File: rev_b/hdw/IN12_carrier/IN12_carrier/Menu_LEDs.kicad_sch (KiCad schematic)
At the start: 28 parts, among them U1002 24AA02-OT, U501 TCA9555RGER

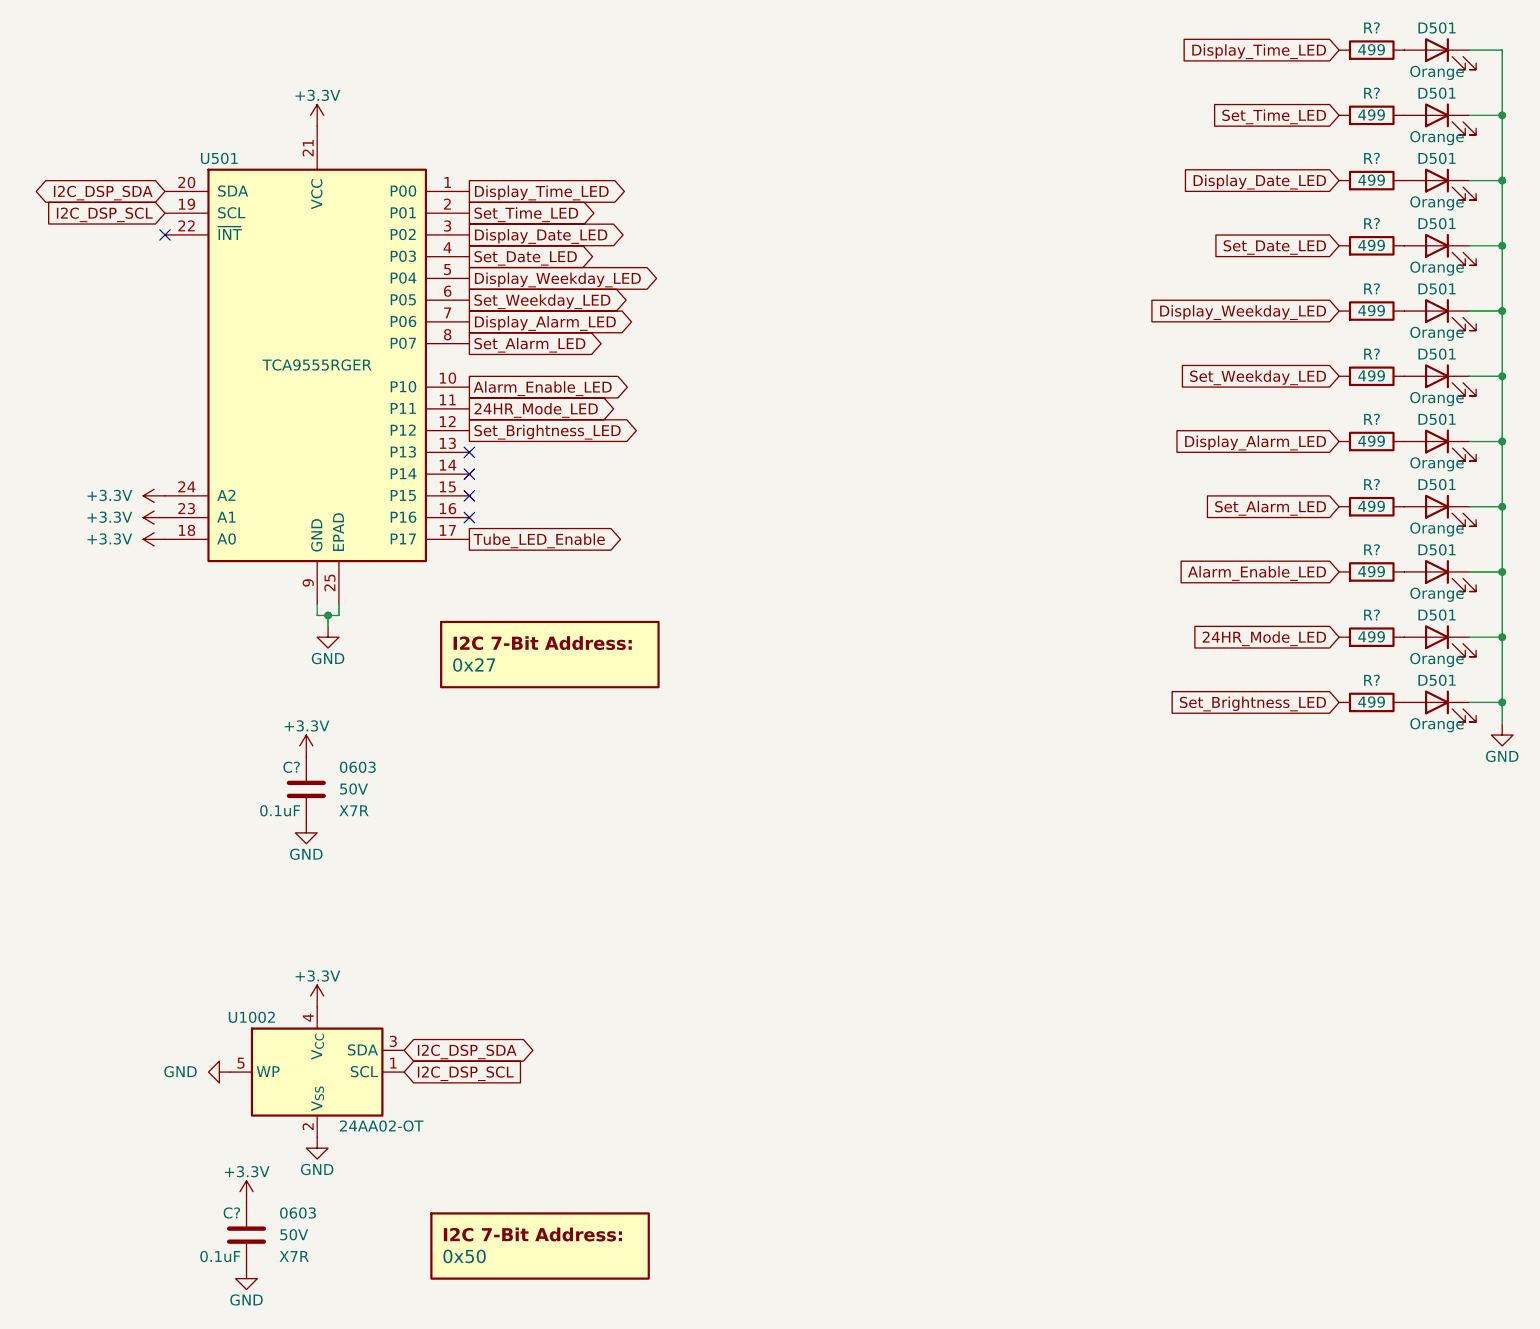
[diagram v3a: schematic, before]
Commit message: added BOM for IN12 carrier, finished routing, some schematic tweaks, adjusted design rules for ERC
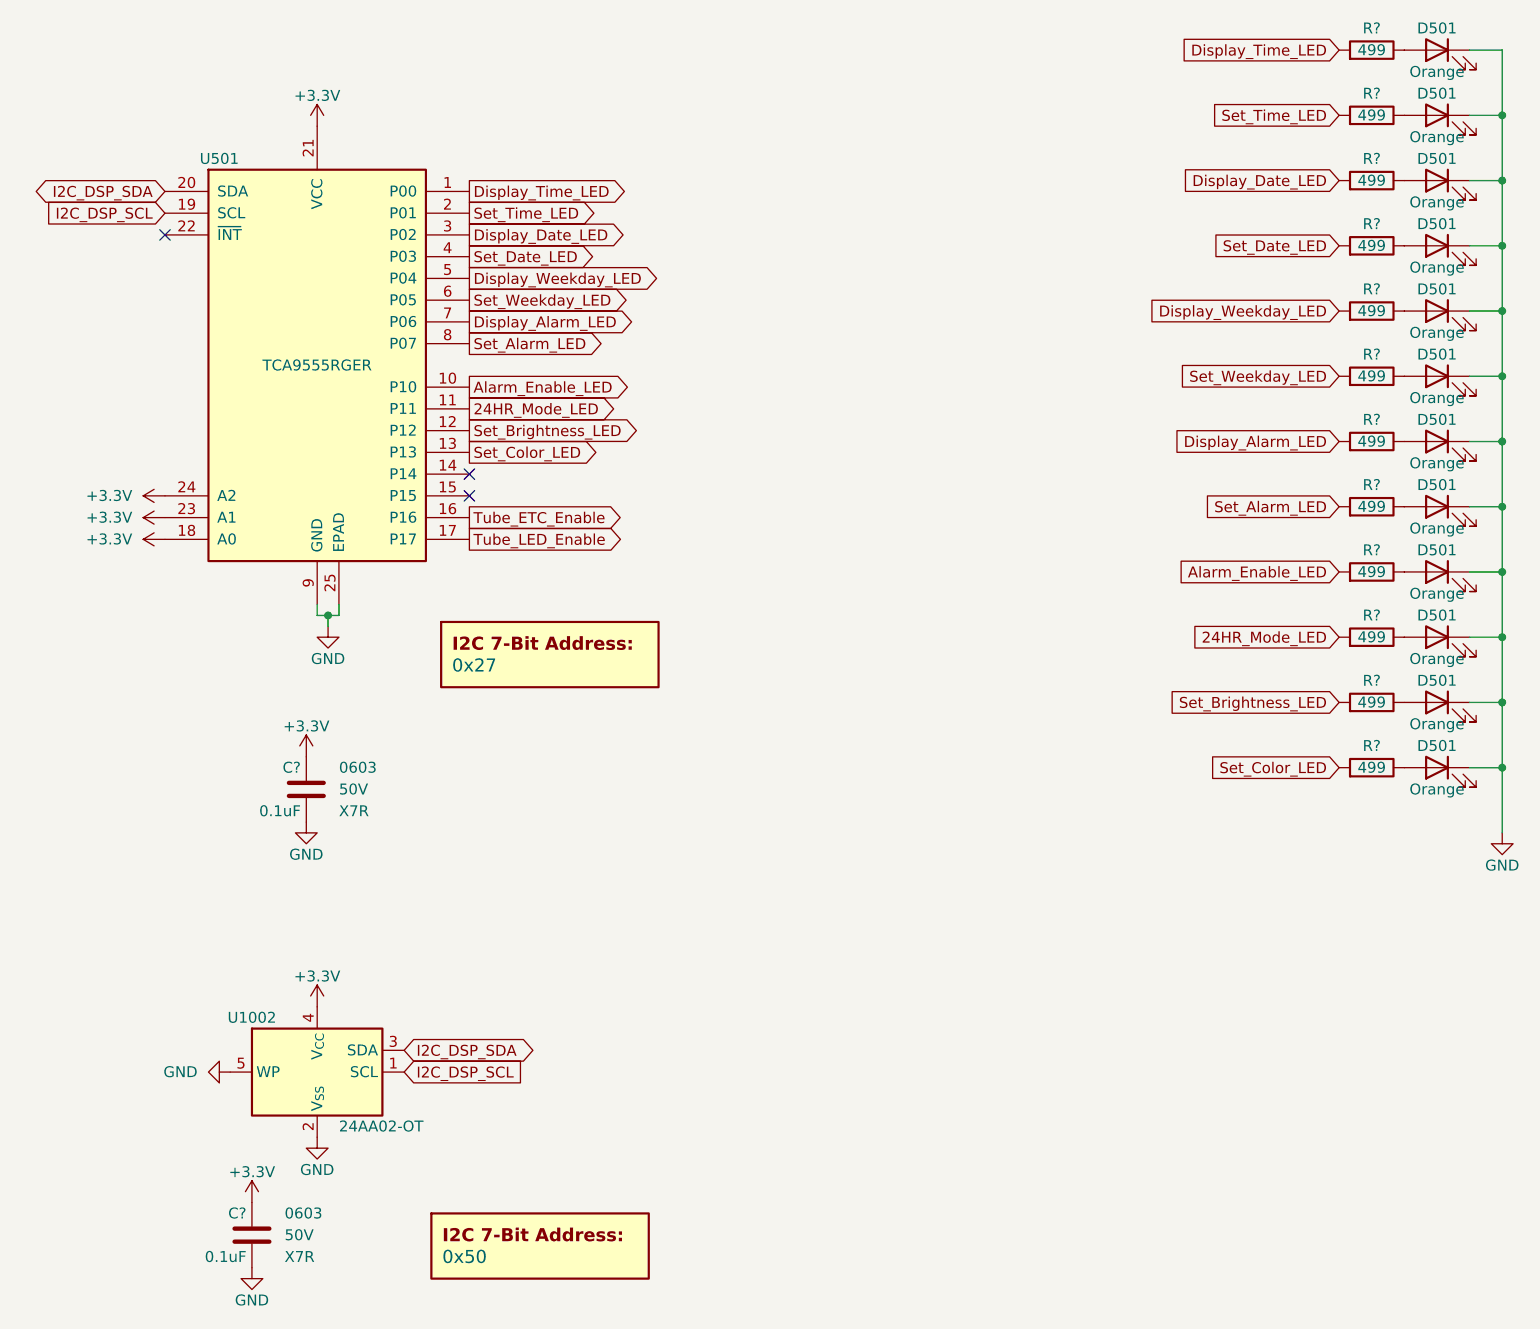
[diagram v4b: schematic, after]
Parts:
- added D501: Orange, LEDs:LED_0603, symbol Device:LED
- added R?: 499, Resistors_SMD:R_0603, symbol Custom_Library:R_Custom
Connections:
- net GND: now also D501.1 (K)
- net Set_Color_LED: now reaches U501.13 (P13)
- net Set_Color_LED: now also R?.1
- net Tube_ETC_Enable: now reaches U501.16 (P16)
- new net: D501.2 (A), R?.2
- no-connect marks 5 -> 3
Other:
- moved on the sheet: C?

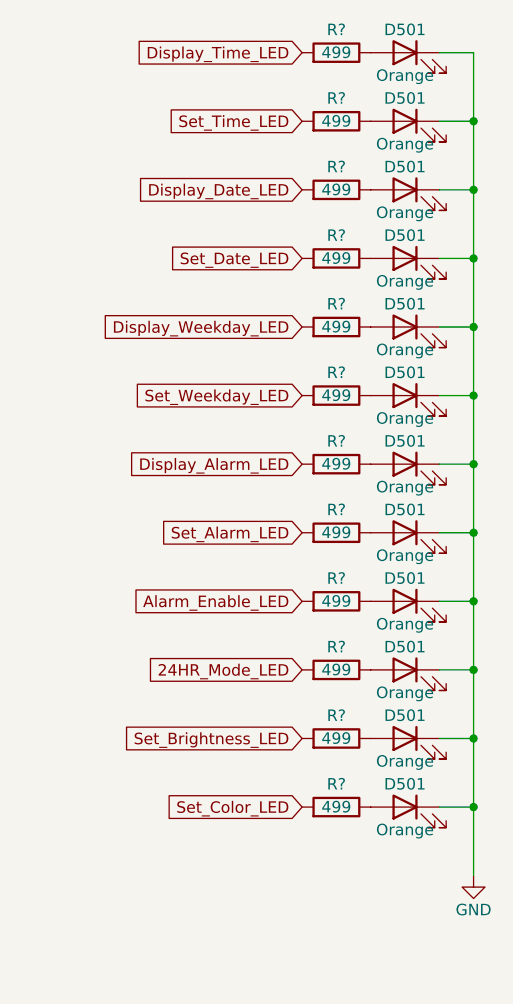
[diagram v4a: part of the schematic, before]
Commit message: assigned digikey pns to IN12 carrier board parts
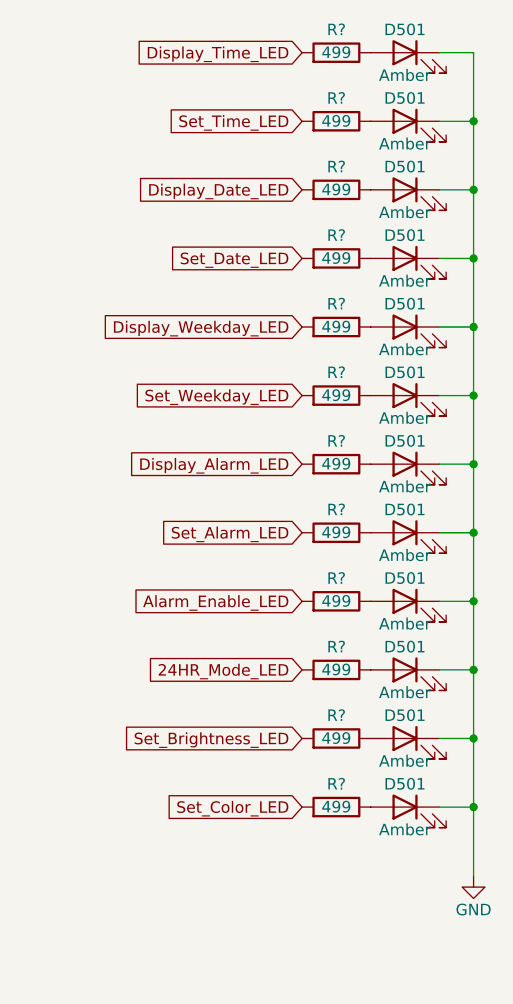
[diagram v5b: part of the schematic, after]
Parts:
- C? (x2): Digi-Key PN (none) -> 1276-CL10B104KB8NNNLCT-ND
- D501: value Orange -> Amber; Digi-Key PN (none) -> 732-150060AS75000CT-ND
- R? (x12): Digi-Key PN (none) -> 541-CRCW0603499RFKEBCT-ND
- U1002: Digi-Key PN (none) -> 24AA02E64T-I/OT
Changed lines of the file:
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@@
       (effects (font (size 1.27 1.27)))
     )
-    (property "Value" "Orange" (at 210.82 82.55 0)
+    (property "Value" "Amber" (at 210.82 82.55 0)
       (effects (font (size 1.27 1.27)))
     )
@@
       (effects (font (size 1.27 1.27)) hide)
     )
-    (property "Digi-Key PN" "" (at 210.82 80.01 0)
+    (property "Digi-Key PN" "732-150060AS75000CT-ND" (at 210.82 80.01 0)
       (effects (font (size 1.27 1.27)) hide)
     )
@@
       (effects (font (size 1.27 1.27)))
     )
-    (property "Value" "Orange" (at 210.82 120.65 0)
+    (property "Value" "Amber" (at 210.82 120.65 0)
       (effects (font (size 1.27 1.27)))
     )
@@
       (effects (font (size 1.27 1.27)) hide)
     )
-    (property "Digi-Key PN" "" (at 210.82 118.11 0)
+    (property "Digi-Key PN" "732-150060AS75000CT-ND" (at 210.82 118.11 0)
       (effects (font (size 1.27 1.27)) hide)
     )
@@
     )
     (property "Datasheet" "http://ww1.microchip.com/downloads/en/DeviceDoc/21709J.pdf" (at 80.01 161.29 0)
+      (effects (font (size 1.27 1.27)) hide)
+    )
+    (property "Digi-Key PN" "24AA02E64T-I/OT" (at 80.01 161.29 0)
       (effects (font (size 1.27 1.27)) hide)
     )
@@
       (effects (font (size 1.27 1.27)))
     )
-    (property "Value" "Orange" (at 210.82 67.31 0)
+    (property "Value" "Amber" (at 210.82 67.31 0)
       (effects (font (size 1.27 1.27)))
     )
@@
       (effects (font (size 1.27 1.27)) hide)
     )
-    (property "Digi-Key PN" "" (at 210.82 64.77 0)
+    (property "Digi-Key PN" "732-150060AS75000CT-ND" (at 210.82 64.77 0)
       (effects (font (size 1.27 1.27)) hide)
     )
@@
       (effects (font (size 1.27 1.27)) hide)
     )
-    (property "Digi-Key PN" "" (at 193.04 72.39 0)
+    (property "Digi-Key PN" "541-CRCW0603499RFKEBCT-ND" (at 193.04 72.39 0)
       (effects (font (size 1.524 1.524)) hide)
     )
@@
       (effects (font (size 1.27 1.27)) hide)
     )
-    (property "Digi-Key PN" "" (at 67.945 115.57 0)
+    (property "Digi-Key PN" "1276-CL10B104KB8NNNLCT-ND" (at 67.945 115.57 0)
       (effects (font (size 1.524 1.524)) hide)
     )
@@
       (effects (font (size 1.27 1.27)) hide)
     )
-    (property "Digi-Key PN" "" (at 193.04 87.63 0)
+    (property "Digi-Key PN" "541-CRCW0603499RFKEBCT-ND" (at 193.04 87.63 0)
       (effects (font (size 1.524 1.524)) hide)
     )
@@
       (effects (font (size 1.27 1.27)))
     )
-    (property "Value" "Orange" (at 210.82 113.03 0)
+    (property "Value" "Amber" (at 210.82 113.03 0)
       (effects (font (size 1.27 1.27)))
     )
@@
       (effects (font (size 1.27 1.27)) hide)
     )
-    (property "Digi-Key PN" "" (at 210.82 110.49 0)
+    (property "Digi-Key PN" "732-150060AS75000CT-ND" (at 210.82 110.49 0)
       (effects (font (size 1.27 1.27)) hide)
     )
@@
       (effects (font (size 1.27 1.27)) hide)
     )
-    (property "Digi-Key PN" "" (at 193.04 118.11 0)
+    (property "Digi-Key PN" "541-CRCW0603499RFKEBCT-ND" (at 193.04 118.11 0)
       (effects (font (size 1.524 1.524)) hide)
     )
@@
       (effects (font (size 1.27 1.27)))
     )
-    (property "Value" "Orange" (at 210.82 128.27 0)
+    (property "Value" "Amber" (at 210.82 128.27 0)
       (effects (font (size 1.27 1.27)))
     )
@@
       (effects (font (size 1.27 1.27)) hide)
     )
-    (property "Digi-Key PN" "" (at 210.82 125.73 0)
+    (property "Digi-Key PN" "732-150060AS75000CT-ND" (at 210.82 125.73 0)
       (effects (font (size 1.27 1.27)) hide)
     )
@@
       (effects (font (size 1.27 1.27)) hide)
     )
-    (property "Digi-Key PN" "" (at 193.04 133.35 0)
+    (property "Digi-Key PN" "541-CRCW0603499RFKEBCT-ND" (at 193.04 133.35 0)
       (effects (font (size 1.524 1.524)) hide)
     )
@@
       (effects (font (size 1.27 1.27)) hide)
     )
-    (property "Digi-Key PN" "" (at 193.04 110.49 0)
+    (property "Digi-Key PN" "541-CRCW0603499RFKEBCT-ND" (at 193.04 110.49 0)
       (effects (font (size 1.524 1.524)) hide)
     )
@@
       (effects (font (size 1.27 1.27)) hide)
     )
-    (property "Digi-Key PN" "" (at 193.04 95.25 0)
+    (property "Digi-Key PN" "541-CRCW0603499RFKEBCT-ND" (at 193.04 95.25 0)
       (effects (font (size 1.524 1.524)) hide)
     )
@@
       (effects (font (size 1.27 1.27)) hide)
     )
-    (property "Digi-Key PN" "" (at 193.04 57.15 0)
+    (property "Digi-Key PN" "541-CRCW0603499RFKEBCT-ND" (at 193.04 57.15 0)
       (effects (font (size 1.524 1.524)) hide)
     )
@@
       (effects (font (size 1.27 1.27)))
     )
-    (property "Value" "Orange" (at 210.82 52.07 0)
+    (property "Value" "Amber" (at 210.82 52.07 0)
       (effects (font (size 1.27 1.27)))
     )
@@
       (effects (font (size 1.27 1.27)) hide)
     )
-    (property "Digi-Key PN" "" (at 210.82 49.53 0)
+    (property "Digi-Key PN" "732-150060AS75000CT-ND" (at 210.82 49.53 0)
       (effects (font (size 1.27 1.27)) hide)
     )
@@
       (effects (font (size 1.27 1.27)))
     )
-    (property "Value" "Orange" (at 210.82 74.93 0)
+    (property "Value" "Amber" (at 210.82 74.93 0)
       (effects (font (size 1.27 1.27)))
     )
@@
       (effects (font (size 1.27 1.27)) hide)
     )
-    (property "Digi-Key PN" "" (at 210.82 72.39 0)
+    (property "Digi-Key PN" "732-150060AS75000CT-ND" (at 210.82 72.39 0)
       (effects (font (size 1.27 1.27)) hide)
     )
@@
       (effects (font (size 1.27 1.27)))
     )
-    (property "Value" "Orange" (at 210.82 90.17 0)
+    (property "Value" "Amber" (at 210.82 90.17 0)
       (effects (font (size 1.27 1.27)))
     )
@@
       (effects (font (size 1.27 1.27)) hide)
     )
-    (property "Digi-Key PN" "" (at 210.82 87.63 0)
+    (property "Digi-Key PN" "732-150060AS75000CT-ND" (at 210.82 87.63 0)
       (effects (font (size 1.27 1.27)) hide)
     )
@@
       (effects (font (size 1.27 1.27)) hide)
     )
-    (property "Digi-Key PN" "" (at 193.04 102.87 0)
+    (property "Digi-Key PN" "541-CRCW0603499RFKEBCT-ND" (at 193.04 102.87 0)
       (effects (font (size 1.524 1.524)) hide)
     )
@@
       (effects (font (size 1.27 1.27)) hide)
     )
-    (property "Digi-Key PN" "" (at 193.04 64.77 0)
+    (property "Digi-Key PN" "541-CRCW0603499RFKEBCT-ND" (at 193.04 64.77 0)
       (effects (font (size 1.524 1.524)) hide)
     )
@@
       (effects (font (size 1.27 1.27)))
     )
-    (property "Value" "Orange" (at 210.82 105.41 0)
+    (property "Value" "Amber" (at 210.82 105.41 0)
       (effects (font (size 1.27 1.27)))
     )
@@
       (effects (font (size 1.27 1.27)) hide)
     )
-    (property "Digi-Key PN" "" (at 210.82 102.87 0)
+    (property "Digi-Key PN" "732-150060AS75000CT-ND" (at 210.82 102.87 0)
       (effects (font (size 1.27 1.27)) hide)
     )
@@
       (effects (font (size 1.27 1.27)) hide)
     )
-    (property "Digi-Key PN" "" (at 193.04 80.01 0)
+    (property "Digi-Key PN" "541-CRCW0603499RFKEBCT-ND" (at 193.04 80.01 0)
       (effects (font (size 1.524 1.524)) hide)
     )
@@
       (effects (font (size 1.27 1.27)))
     )
-    (property "Value" "Orange" (at 210.82 59.69 0)
+    (property "Value" "Amber" (at 210.82 59.69 0)
       (effects (font (size 1.27 1.27)))
     )
@@
       (effects (font (size 1.27 1.27)) hide)
     )
-    (property "Digi-Key PN" "" (at 210.82 57.15 0)
+    (property "Digi-Key PN" "732-150060AS75000CT-ND" (at 210.82 57.15 0)
       (effects (font (size 1.27 1.27)) hide)
     )
@@
       (effects (font (size 1.27 1.27)) hide)
     )
-    (property "Digi-Key PN" "" (at 193.04 125.73 0)
+    (property "Digi-Key PN" "541-CRCW0603499RFKEBCT-ND" (at 193.04 125.73 0)
       (effects (font (size 1.524 1.524)) hide)
     )
@@
       (effects (font (size 1.27 1.27)))
     )
-    (property "Value" "Orange" (at 210.82 97.79 0)
+    (property "Value" "Amber" (at 210.82 97.79 0)
       (effects (font (size 1.27 1.27)))
     )
@@
       (effects (font (size 1.27 1.27)) hide)
     )
-    (property "Digi-Key PN" "" (at 210.82 95.25 0)
+    (property "Digi-Key PN" "732-150060AS75000CT-ND" (at 210.82 95.25 0)
       (effects (font (size 1.27 1.27)) hide)
     )
@@
       (effects (font (size 1.27 1.27)) hide)
     )
-    (property "Digi-Key PN" "" (at 193.04 49.53 0)
+    (property "Digi-Key PN" "541-CRCW0603499RFKEBCT-ND" (at 193.04 49.53 0)
       (effects (font (size 1.524 1.524)) hide)
     )
@@
       (effects (font (size 1.27 1.27)))
     )
-    (property "Value" "Orange" (at 210.82 44.45 0)
+    (property "Value" "Amber" (at 210.82 44.45 0)
       (effects (font (size 1.27 1.27)))
     )
@@
       (effects (font (size 1.27 1.27)) hide)
     )
-    (property "Digi-Key PN" "" (at 210.82 41.91 0)
+    (property "Digi-Key PN" "732-150060AS75000CT-ND" (at 210.82 41.91 0)
       (effects (font (size 1.27 1.27)) hide)
     )
@@
       (effects (font (size 1.27 1.27)) hide)
     )
-    (property "Digi-Key PN" "" (at 61.595 167.64 0)
-      (effects (font (size 1.524 1.524)) hide)
-    )
+    (property "Digi-Key PN" "1276-CL10B104KB8NNNLCT-ND" (at 61.595 167.64 0)
+      (effects (font (size 1.524 1.524)) hide)
+    )
